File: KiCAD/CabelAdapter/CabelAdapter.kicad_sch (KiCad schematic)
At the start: 20 parts, among them J1 8P8C, J10 Conn_02x08_Odd_Even, J11 Conn_Coaxial, J12 Conn_01x04_Pin, J13 Conn_01x08_Pin, J14 Conn_Coaxial, J15 Screw_Terminal_01x08, J16 Conn_Coaxial, J17 Conn_01x04_Pin, J18 Conn_Coaxial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

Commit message: added cable adapter pcb
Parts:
- J1: footprint (none) -> Library:RJ45_Amphenol_54602-x08_Horizontal_Custom
- J10, J3, J4, J5, J6, J7, J8, J9: footprint (none) -> Connector_PinSocket_2.54mm:PinSocket_2x08_P2.54mm_Vertical
- J11, J14, J16, J18: footprint (none) -> Library:BNC_Connector
- J12, J17: footprint (none) -> Connector_PinSocket_2.54mm:PinSocket_1x04_P2.54mm_Vertical
- J13: footprint (none) -> Connector_PinSocket_2.54mm:PinSocket_1x08_P2.54mm_Vertical
- J15: footprint (none) -> Library:ScrewConnector8
- J19, J20: footprint (none) -> TerminalBlock_MetzConnect:TerminalBlock_MetzConnect_Type055_RT01502HDWU_1x02_P5.00mm_Horizontal
- J2: footprint (none) -> Connector_PinSocket_2.54mm:PinSocket_1x06_P2.54mm_Vertical
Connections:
- net +5V: now also J3.15 (Pin_15), J5.15 (Pin_15), J7.15 (Pin_15), J9.15 (Pin_15); no longer J3.1 (Pin_1), J5.1 (Pin_1), J7.1 (Pin_1), J9.1 (Pin_1)
- net CS: now also J3.13 (Pin_13), J5.13 (Pin_13), J7.13 (Pin_13), J9.13 (Pin_13); no longer J3.3 (Pin_3), J5.3 (Pin_3), J7.3 (Pin_3), J9.3 (Pin_3)
- net GND: now also J3.5 (Pin_5), J5.5 (Pin_5), J7.5 (Pin_5), J9.5 (Pin_5); no longer J3.11 (Pin_11), J5.11 (Pin_11), J7.11 (Pin_11), J9.11 (Pin_11)
- net MOSI: now also J3.9 (Pin_9), J5.9 (Pin_9), J7.9 (Pin_9), J9.9 (Pin_9); no longer J3.7 (Pin_7), J5.7 (Pin_7), J7.7 (Pin_7), J9.7 (Pin_7)
- net SCK: now also J3.11 (Pin_11), J5.11 (Pin_11), J7.11 (Pin_11), J9.11 (Pin_11); no longer J3.5 (Pin_5), J5.5 (Pin_5), J7.5 (Pin_5), J9.5 (Pin_5)
- net SHUTDOWN: now also J3.7 (Pin_7), J5.7 (Pin_7), J7.7 (Pin_7), J9.7 (Pin_7); no longer J3.9 (Pin_9), J5.9 (Pin_9), J7.9 (Pin_9), J9.9 (Pin_9)
- net SIGNAL_1: now also J3.3 (Pin_3), J5.3 (Pin_3), J7.3 (Pin_3), J9.3 (Pin_3); no longer J3.13 (Pin_13), J5.13 (Pin_13), J7.13 (Pin_13), J9.13 (Pin_13)
- net SIGNAL_2: now also J3.1 (Pin_1), J5.1 (Pin_1), J7.1 (Pin_1), J9.1 (Pin_1); no longer J3.15 (Pin_15), J5.15 (Pin_15), J7.15 (Pin_15), J9.15 (Pin_15)

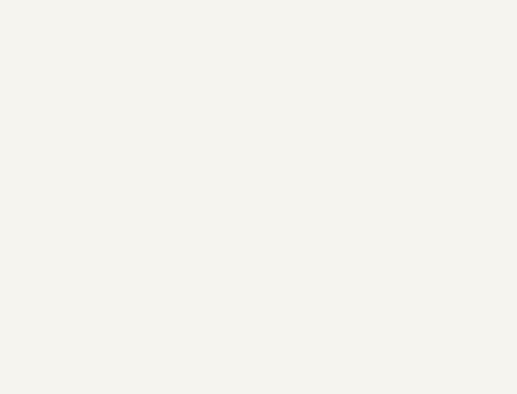
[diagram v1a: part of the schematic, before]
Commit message: added mounting holes
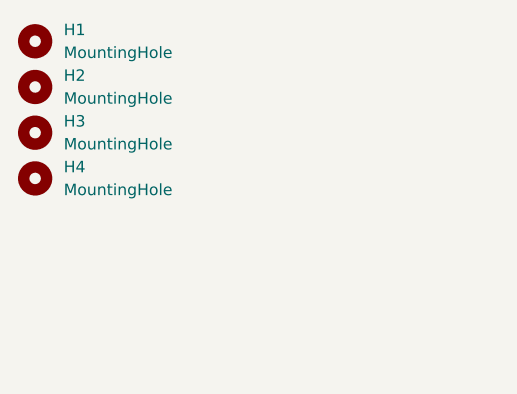
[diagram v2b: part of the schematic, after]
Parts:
- added H1, H2, H3, H4: MountingHole, MountingHole:MountingHole_3.2mm_M3, symbol Mechanical:MountingHole
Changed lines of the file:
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@@
+    )
+  )
+  (symbol (lib_id "Mechanical:MountingHole") (at 20.955 19.685 0) (unit 1)
+    (in_bom yes) (on_board yes) (dnp no) (fields_autoplaced)
+    (property "Reference" "H1" (at 24.13 18.415 0)
+      (effects (font (size 1.27 1.27)) (justify left))
+    )
+    (property "Value" "MountingHole" (at 24.13 20.955 0)
+      (effects (font (size 1.27 1.27)) (justify left))
+    )
+    (property "Footprint" "MountingHole:MountingHole_3.2mm_M3" (at 20.955 19.685 0)
+      (effects (font (size 1.27 1.27)) hide)
+    )
+    (property "Datasheet" "~" (at 20.955 19.685 0)
+      (effects (font (size 1.27 1.27)) hide)
+    )
+    (instances
+      (project "CabelAdapter"
+        (path "/fc02849e-c7bc-4e73-8029-80464fa46019"
+          (reference "H1") (unit 1)
+        )
+      )
     )
   )
@@
         (path "/fc02849e-c7bc-4e73-8029-80464fa46019"
           (reference "J16") (unit 1)
+        )
+      )
+    )
+  )
+  (symbol (lib_id "Mechanical:MountingHole") (at 20.955 34.925 0) (unit 1)
+    (in_bom yes) (on_board yes) (dnp no) (fields_autoplaced)
+    (property "Reference" "H4" (at 24.13 33.655 0)
+      (effects (font (size 1.27 1.27)) (justify left))
+    )
+    (property "Value" "MountingHole" (at 24.13 36.195 0)
+      (effects (font (size 1.27 1.27)) (justify left))
+    )
+    (property "Footprint" "MountingHole:MountingHole_3.2mm_M3" (at 20.955 34.925 0)
+      (effects (font (size 1.27 1.27)) hide)
+    )
+    (property "Datasheet" "~" (at 20.955 34.925 0)
+      (effects (font (size 1.27 1.27)) hide)
+    )
+    (instances
+      (project "CabelAdapter"
+        (path "/fc02849e-c7bc-4e73-8029-80464fa46019"
+          (reference "H4") (unit 1)
         )
       )
@@
     )
   )
+  (symbol (lib_id "Mechanical:MountingHole") (at 20.955 24.765 0) (unit 1)
+    (in_bom yes) (on_board yes) (dnp no) (fields_autoplaced)
+    (property "Reference" "H2" (at 24.13 23.495 0)
+      (effects (font (size 1.27 1.27)) (justify left))
+    )
+    (property "Value" "MountingHole" (at 24.13 26.035 0)
+      (effects (font (size 1.27 1.27)) (justify left))
+    )
+    (property "Footprint" "MountingHole:MountingHole_3.2mm_M3" (at 20.955 24.765 0)
+      (effects (font (size 1.27 1.27)) hide)
+    )
+    (property "Datasheet" "~" (at 20.955 24.765 0)
+      (effects (font (size 1.27 1.27)) hide)
+    )
+    (instances
+      (project "CabelAdapter"
+        (path "/fc02849e-c7bc-4e73-8029-80464fa46019"
+          (reference "H2") (unit 1)
+        )
+      )
+    )
+  )
   (symbol (lib_id "power:+5V") (at 91.44 137.795 0) (unit 1)
     (in_bom yes) (on_board yes) (dnp no) (fields_autoplaced)
@@
         )
       )
+    )
+  )
+  (symbol (lib_id "Mechanical:MountingHole") (at 20.955 29.845 0) (unit 1)
+    (in_bom yes) (on_board yes) (dnp no) (fields_autoplaced)
+    (property "Reference" "H3" (at 24.13 28.575 0)
+      (effects (font (size 1.27 1.27)) (justify left))
+    )
+    (property "Value" "MountingHole" (at 24.13 31.115 0)
+      (effects (font (size 1.27 1.27)) (justify left))
+    )
+    (property "Footprint" "MountingHole:MountingHole_3.2mm_M3" (at 20.955 29.845 0)
+      (effects (font (size 1.27 1.27)) hide)
+    )
+    (property "Datasheet" "~" (at 20.955 29.845 0)
+      (effects (font (size 1.27 1.27)) hide)
+    )
+    (instances
+      (project "CabelAdapter"
+        (path "/fc02849e-c7bc-4e73-8029-80464fa46019"
+          (reference "H3") (unit 1)
+        )
+      )
